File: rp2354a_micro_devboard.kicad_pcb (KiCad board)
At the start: 2 copper layers, 36.4 x 59.3 mm, 33 parts, among them J1 USB_C_Receptacle_USB2.0_16P, J2 01x20_PinHeader_P2.54mm, J3 01x20_PinHeader_P2.54mm, J4 SWD_XH_3p, U1 HT7533-1, U2 RP2354A, Y1 YIC 12M10PB

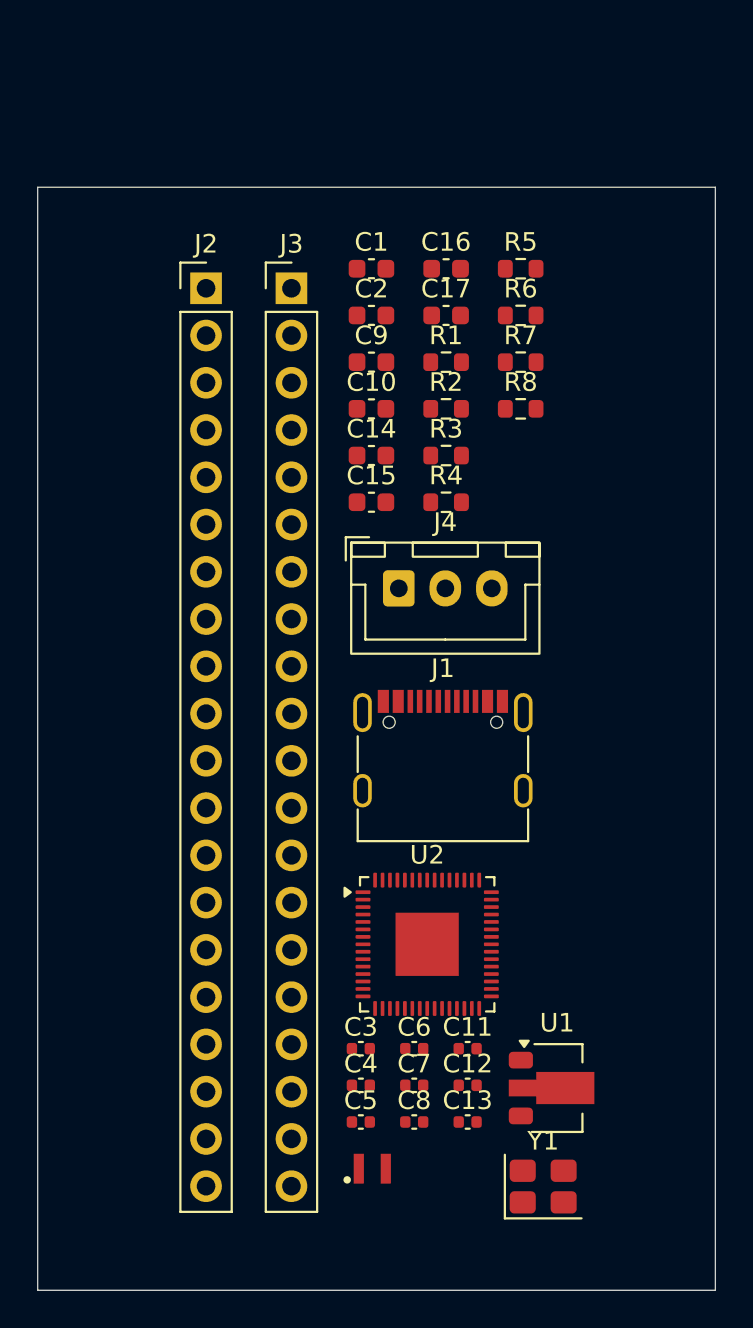
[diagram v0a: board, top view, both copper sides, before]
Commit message: feat: add battely charge&source. but kind to 1S-LiPo only.
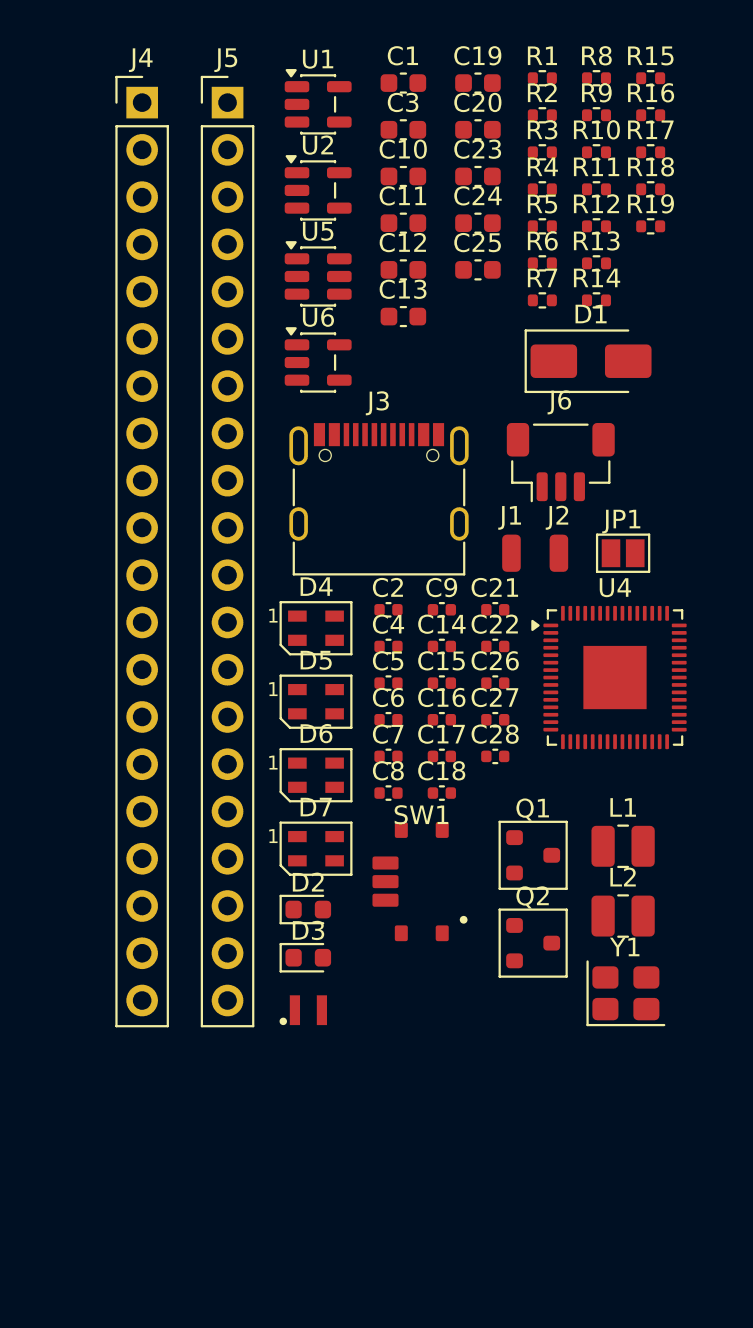
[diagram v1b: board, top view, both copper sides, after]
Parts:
- added C18: 100n, Capacitor_SMD:C_0402_1005Metric, F.Cu at (124.3, 80.9)
- added C19: 4.7u, Capacitor_SMD:C_0603_1608Metric, F.Cu at (126.2, 42.7)
- added C20: 4.7u, Capacitor_SMD:C_0603_1608Metric, F.Cu at (126.2, 45.2)
- added C21: 100n, Capacitor_SMD:C_0402_1005Metric, F.Cu at (127.1, 71.0)
- added C22: 100n, Capacitor_SMD:C_0402_1005Metric, F.Cu at (127.1, 73.0)
- added C23: 4.7u, Capacitor_SMD:C_0603_1608Metric, F.Cu at (126.2, 47.8)
- added C24: 4.7u, Capacitor_SMD:C_0603_1608Metric, F.Cu at (126.2, 50.3)
- added C25: 4.7u, Capacitor_SMD:C_0603_1608Metric, F.Cu at (126.2, 52.8)
- added C26: 15p, Capacitor_SMD:C_0402_1005Metric, F.Cu at (127.1, 75.0)
- added C27: 15p, Capacitor_SMD:C_0402_1005Metric, F.Cu at (127.1, 77.0)
- added C28: 100n, Capacitor_SMD:C_0402_1005Metric, F.Cu at (127.1, 78.9)
- added D1: SS32, Diode_SMD:D_SMA, F.Cu at (132.3, 57.7)
- added D2: Red_LED, LED_SMD:LED_0603_1608Metric, F.Cu at (117.1, 87.2)
- added D3: Red_LED, LED_SMD:LED_0603_1608Metric, F.Cu at (117.1, 89.7)
- added D4: SK6805, LED_SMD:LED_SK6805_PLCC4_2.4x2.7mm_P1.3mm, F.Cu at (117.5, 72.0)
- added D5: SK6805, LED_SMD:LED_SK6805_PLCC4_2.4x2.7mm_P1.3mm, F.Cu at (117.5, 76.0)
- added D6: SK6805, LED_SMD:LED_SK6805_PLCC4_2.4x2.7mm_P1.3mm, F.Cu at (117.5, 79.9)
- added D7: SK6805, LED_SMD:LED_SK6805_PLCC4_2.4x2.7mm_P1.3mm, F.Cu at (117.5, 83.9)
- added J5: 01x20_PinHeader_P2.54mm, Connector_PinHeader_2.54mm:PinHeader_1x20_P2.54mm_Vertical, F.Cu at (112.7, 43.8)
- added J6: SWD_SH_3p, Connector_JST:JST_SH_BM03B-SRSS-TB_1x03-1MP_P1.00mm_Vertical, F.Cu at (130.7, 63.1)
- added JP1: VBAT_ADC, Jumper:SolderJumper-2_P1.3mm_Open_Pad1.0x1.5mm, F.Cu at (134.0, 68.0)
- added L2: 1uH, Inductor_SMD:L_1008_2520Metric, F.Cu at (134.0, 87.5)
- added L3: 3.3uH, PCM_SparkFun-Coil:0806_Polarized, F.Cu at (117.1, 92.6)
- added Q1: AO3407A, PCM_Package_TO_SOT_SMD_AKL:SOT-23, F.Cu at (129.2, 84.2)
- added Q2: AO3407A, PCM_Package_TO_SOT_SMD_AKL:SOT-23, F.Cu at (129.2, 89.0)
- added R10: 330, Resistor_SMD:R_0402_1005Metric, F.Cu at (132.6, 46.5)
- added R11: 330, Resistor_SMD:R_0402_1005Metric, F.Cu at (132.6, 48.4)
- added R12: 27, Resistor_SMD:R_0402_1005Metric, F.Cu at (132.6, 50.4)
- added R13: 1k, Resistor_SMD:R_0402_1005Metric, F.Cu at (132.6, 52.4)
- added R14: 27, Resistor_SMD:R_0402_1005Metric, F.Cu at (132.6, 54.4)
- added R15: 27, Resistor_SMD:R_0402_1005Metric, F.Cu at (135.5, 42.5)
- added R16: 1k, Resistor_SMD:R_0402_1005Metric, F.Cu at (135.5, 44.5)
- added R17: 1k, Resistor_SMD:R_0402_1005Metric, F.Cu at (135.5, 46.5)
- added R18: 150k, Resistor_SMD:R_0402_1005Metric, F.Cu at (135.5, 48.4)
- added R19: 150k, Resistor_SMD:R_0402_1005Metric, F.Cu at (135.5, 50.4)
- added R9: 5k1, Resistor_SMD:R_0402_1005Metric, F.Cu at (132.6, 44.5)
- added SW1: HX_MINI_MSK12CO2, Download_Lib:HX_MINI_MSK12CO2, F.Cu at (123.2, 85.7)
- added U4: RP2354A, Package_DFN_QFN:QFN-60-1EP_7x7mm_P0.4mm_EP3.4x3.4mm, F.Cu at (133.6, 74.7)
- added U5: USBLC6-2SC6, Package_TO_SOT_SMD:SOT-23-6, F.Cu at (117.6, 53.1)
- added U6: TPS613222ADBV, Package_TO_SOT_SMD:SOT-23-5, F.Cu at (117.6, 57.8)
- C1: value 10u -> 22u
- C11, C12, C3: value 100n -> 22u; footprint Capacitor_SMD:C_0402_1005Metric -> Capacitor_SMD:C_0603_1608Metric
- C13: value 100n -> 4.7u; footprint Capacitor_SMD:C_0402_1005Metric -> Capacitor_SMD:C_0603_1608Metric
- C14, C15, C9: value 4.7u -> 100n; footprint Capacitor_SMD:C_0603_1608Metric -> Capacitor_SMD:C_0402_1005Metric
- C16, C17: value 15p -> 100n; footprint Capacitor_SMD:C_0603_1608Metric -> Capacitor_SMD:C_0402_1005Metric
- C2: value 10u -> 15p; footprint Capacitor_SMD:C_0603_1608Metric -> Capacitor_SMD:C_0402_1005Metric
- J1: value USB_C_Receptacle_USB2.0_16P -> BAT+; footprint Connector_USB:USB_C_Receptacle_G-Switch_GT-USB-7010ASV -> Connector_Wire:SolderWirePad_1x01_SMD_1x2mm
- J2: value 01x20_PinHeader_P2.54mm -> BAT-; footprint Connector_PinHeader_2.54mm:PinHeader_1x20_P2.54mm_Vertical -> Connector_Wire:SolderWirePad_1x01_SMD_1x2mm
- J3: value 01x20_PinHeader_P2.54mm -> USB_C_Receptacle_USB2.0_16P; footprint Connector_PinHeader_2.54mm:PinHeader_1x20_P2.54mm_Vertical -> Connector_USB:USB_C_Receptacle_G-Switch_GT-USB-7010ASV
- J4: value SWD_XH_3p -> 01x20_PinHeader_P2.54mm; footprint Connector_JST:JST_XH_B3B-XH-A_1x03_P2.50mm_Vertical -> Connector_PinHeader_2.54mm:PinHeader_1x20_P2.54mm_Vertical
- L1: value 3.3uH -> 1uH; footprint PCM_SparkFun-Coil:0806_Polarized -> Inductor_SMD:L_1008_2520Metric
- R1, R2, R4: value 1k -> 5k1; footprint Resistor_SMD:R_0603_1608Metric -> Resistor_SMD:R_0402_1005Metric
- R3: value 33 -> 150k; footprint Resistor_SMD:R_0603_1608Metric -> Resistor_SMD:R_0402_1005Metric
- R5, R6: value 22 -> 150k; footprint Resistor_SMD:R_0603_1608Metric -> Resistor_SMD:R_0402_1005Metric
- R7: value 1k -> 33k2; footprint Resistor_SMD:R_0603_1608Metric -> Resistor_SMD:R_0402_1005Metric
- R8: footprint Resistor_SMD:R_0603_1608Metric -> Resistor_SMD:R_0402_1005Metric
- U1: value HT7533-1 -> TMI3112H; footprint Package_TO_SOT_SMD:SOT-89-3 -> Package_TO_SOT_SMD:SOT-23-5
- U2: value RP2354A -> MCP73832-2-OT; footprint Package_DFN_QFN:QFN-60-1EP_7x7mm_P0.4mm_EP3.4x3.4mm -> Package_TO_SOT_SMD:SOT-23-5
- moved U1 54.4 mm to (117.6, 43.9)
- moved C3 49.4 mm to (122.2, 45.2)
- moved C11 44.5 mm to (122.2, 50.3)
- moved C12 44.0 mm to (122.2, 52.8)
- moved C13 43.4 mm to (122.2, 55.3)
- moved U2 40.9 mm to (117.6, 48.5)
- moved J4 29.5 mm to (108.2, 43.8)
- moved C16 24.2 mm to (124.3, 77.0)
- moved J2 23.7 mm to (130.6, 68.0)
- moved C17 23.7 mm to (124.3, 78.9)
- moved C4 23.6 mm to (121.4, 73.0)
- moved C5 23.6 mm to (121.4, 75.0)
- moved L1 22.0 mm to (134.0, 83.8)
- moved R8 18.2 mm to (132.6, 42.5)
- moved C6 17.7 mm to (121.4, 77.0)
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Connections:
- C1 pad 1: VBUS -> IO_VBUS
- C10 pad 1: GND -> Net-(Q2-D)
- C10 pad 2: Net-(U2-VREG_AVDD) -> GND
- C11 pad 1: +3V3 -> IO_VBUS
- C12 pad 1: Net-(U2-VREG_FB) -> IO_VBUS
- C13 pad 1: Net-(U2-VREG_FB) -> GND
- C13 pad 2: GND -> USB_VBUS
- C14 pad 1: Net-(U2-VREG_FB) -> GND
- C14 pad 2: GND -> IO_VBUS
- C15 pad 1: Net-(U2-VREG_FB) -> GND
- C15 pad 2: GND -> IO_VBUS
- C16 pad 2: Net-(U2-XIN) -> IO_VBUS
- C17 pad 2: Net-(C17-Pad2) -> IO_VBUS
- C2 pad 1: +3V3 -> Net-(U1-FB)
- C2 pad 2: GND -> +3V3
- C3 pad 2: GND -> Net-(C3-Pad2)
- C4 pad 2: GND -> Net-(C3-Pad2)
- C5 pad 2: GND -> Net-(C3-Pad2)
- C6 pad 2: GND -> Net-(C3-Pad2)
- C7 pad 2: GND -> Net-(C3-Pad2)
- C8 pad 2: GND -> Net-(C3-Pad2)
- C9 pad 1: GND -> +3V3
- C9 pad 2: +3V3 -> Net-(C3-Pad2)
- J2 pad 1: VBUS -> GND
- J4 pad 1: SWDIO -> GND
- J4 pad 2: GND -> GPIO0
- J4 pad 3: SWCLK -> GPIO1
- L1 pad 1: Net-(U2-VREG_LX) -> Net-(U1-LX)
- L1 pad 2: Net-(U2-VREG_FB) -> +3V3
- R1 pad 1: GND -> Net-(D2-A)
- R1 pad 2: Net-(J1-CC1) -> +3V3
- R2 pad 2: Net-(J1-CC2) -> Net-(J3-CC1)
- R3 pad 1: +3V3 -> Net-(U1-FB)
- R3 pad 2: Net-(U2-VREG_AVDD) -> +3V3
- R4 pad 2: Net-(SW1-A) -> Net-(J3-CC2)
- R5 pad 1: Net-(U2-USB_DM) -> Net-(Q1-G)
- R5 pad 2: D- -> Net-(SW1-B)
- R6 pad 1: Net-(U2-USB_DP) -> USB_VBUS
- R6 pad 2: D+ -> GND
- R7 pad 1: GND -> Net-(U1-FB)
- R7 pad 2: Net-(SW2-A) -> GND
- R8 pad 1: Net-(C17-Pad2) -> Net-(D3-K)
- R8 pad 2: Net-(U2-XOUT) -> Net-(U2-V_{BAT})
- U1 pad 1: GND -> IO_VBUS
- U1 pad 2: VBUS -> GND
- U1 pad 3: +3V3 -> Net-(U1-LX)
- U2 pad 1: +3V3 -> BAT_CELL
- U2 pad 2: GPIO0 -> GND
- U2 pad 3: GPIO1 -> Net-(U2-V_{BAT})
- U2 pad 4: GPIO2 -> USB_VBUS
- U2 pad 5: GPIO3 -> Net-(U2-PROG)
- Y1 pad 1: Net-(C17-Pad2) -> Net-(C27-Pad2)
- Y1 pad 3: Net-(U2-XIN) -> Net-(U4-XIN)
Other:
- board outline removed
